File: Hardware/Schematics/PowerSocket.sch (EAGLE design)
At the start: 74 parts, among them T1 BT138-V, T2 BT138-V, T3 BT138-V, T4 BT138-V, T5 BT138-V, T6 BT138-V

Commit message: New board layout
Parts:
- removed ACIN-NULL, ACIN-PHASE, ACOUT-NULL, ACOUT-NULL1, ACOUT-NULL2, ACOUT-PHASE, ACOUT-PHASE1, ACOUT-PHASE2: -, wirepad:3,81/1,4
- removed BUTTON_LED+: BUTTON_VCC, wirepad:2,15/1,0
- removed BUTTON_LED+1, BUTTON_LED+2, BUTTON_LED-, BUTTON_LED-1, BUTTON_LED-2, BUTTON_SWITCH1, BUTTON_SWITCH3, BUTTON_SWITCH5: -, wirepad:2,15/1,0
- removed U$1, U$3, U$4: ACS710, PowerSocket:ACS710
- added AMP1, AMP2, AMP3: ACS710, PowerSocket:ACS710
- added BUTTON1_VCC: (no value), wirepad:2,15/1,0
- added BUTTON2_VCC, BUTTON3_VCC, LED1, LED2, LED3, SWITCH1, SWITCH2, SWITCH3: -, wirepad:2,15/1,0
- added NULL, NULL1-OUT, NULL2-OUT, NULL3-OUT, PHASE, PHASE1-OUT, PHASE2-OUT, PHASE3-OUT: -, wirepad:3,81/1,4
- added R24: 0, eagle-ltspice:RR2010
- R14, R18: device rcl:C-EUC0805 -> rcl:R-EU_R0805
- T1, T2, T3, T4, T5, T6: value BT138-V -> BT138-H; device triac:BT138-V -> triac:BT138-H
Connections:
- net N$25 renamed GATE2
- net N$3 renamed VOLTMETER
- removed net N$15 (its old number): BUTTON_LED-.P, R7.1
- removed net N$2 (its old number): R1.1, RESET.P1, U$2.EN
- removed net N$36 (its old number): ACOUT-PHASE1.P, U$3.IP-, U$3.IP-1, U$3.IP-2, U$3.IP-3
- removed net N$40: U$3.NFAULT
- removed net N$42 (its old number): OK5.C, R16.2
- removed net N$43: OK5.A2, R17.1
- removed net N$45: ACIN-NULL.P, R5.1, T1.A1, T3.A1, T5.A1
- removed net N$46: OK6.C, R18.1
- removed net N$47: OK6.A2, R19.1
- removed net N$49: R19.2, T6.A2, U$4.IP+, U$4.IP+1, U$4.IP+2, U$4.IP+3
- removed net N$50: U$4.NFAULT
- removed net N$51: ACIN-PHASE.P, D1.C, T2.A1, T4.A1, T6.A1
- removed net N$52: R22.2, U$2.IO5
- removed net N$53: R15.2, T4.A2, U$3.IP+, U$3.IP+1, U$3.IP+2, U$3.IP+3
- removed net N$54: R16.1, R18.2, U$2.IO27
- removed net N$55: C9.2, U$1.FILTER
- removed net N$60: C10.2, U$1.VZCR
- removed net N$62: C1.2, U$3.FILTER
- removed net N$63: C4.2, U$3.VZCR
- removed net N$64: C5.2, U$4.FILTER
- removed net N$65: C6.2, U$4.VZCR
- new net AMP1: AMP1.VIOUT, U$2.IO34
- new net AMP2: AMP2.VIOUT, U$2.IO35
- new net AMP3: AMP3.VIOUT, U$2.IO32
- new net BUTTON1: R8.1, SWITCH1.P, U$2.IO22
- new net BUTTON2: R21.1, SWITCH2.P, U$2.IO23
- new net BUTTON3: R23.1, SWITCH3.P, U$2.IO5
- new net GATE1: R3.2, R9.2, U$2.IO25
- new net GATE3: R16.1, R18.1, U$2.IO27
- new net LED1: R7.2, U$2.IO19
- new net LED2: R20.2, U$2.IO18
- new net LED3: R22.2, U$2.IO17
- new net N$24: FLASH.P, FLASH.P1, R2.2, U$2.IO0
- new net N$30: AMP2.VZCR, C4.1
- new net N$66: R1.1, RESET.P, RESET.P1, U$2.EN
- new net NULL: NULL.P, R5.1, T2.A1, T4.A1, T6.A1
- new net PHASE: PHASE.P, R24.2, T1.A1, T3.A1, T5.A1
- new net PHASE1: AMP1.IP+, AMP1.IP+1, AMP1.IP+2, AMP1.IP+3, R10.2, T1.A2
- new net PHASE2: AMP2.IP+, AMP2.IP+1, AMP2.IP+2, AMP2.IP+3, R15.2, T3.A2
- new net PHASE3: AMP3.IP+, AMP3.IP+1, AMP3.IP+2, AMP3.IP+3, R19.2, T5.A2
- net GND: now also AMP1.FAULT_EN, AMP1.GND, AMP2.FAULT_EN, AMP2.GND, AMP3.FAULT_EN, AMP3.GND, C1.2, C10.2, C11.2, C12.2, C13.2, C4.2, C5.2, C6.2, C9.2, FLASH.S, R21.2, R23.2, R8.2, RESET.S1; no longer C1.1, C10.1, C11.1, C12.1, C13.1, C4.1, C5.1, C6.1, C9.1, R21.1, R23.1, R8.1, U$1.FAULT_EN, U$1.GND, U$3.FAULT_EN, U$3.GND, U$4.FAULT_EN, U$4.GND
- net N$1: now also OK1.C, R9.1; no longer ACOUT-NULL.P, R4.2, T1.A2
- net N$10: now also AMP3.IP-, AMP3.IP-1, AMP3.IP-2, AMP3.IP-3, PHASE3-OUT.P; no longer OK2.C, R9.1
- net N$11: now also LED3.P, R22.1; no longer U$2.IO35, U$3.VIOUT
- net N$12: now also AMP1.VZCR, C10.1; no longer U$1.VIOUT, U$2.IO34
- net N$13: now also AMP1.FILTER, C9.1; no longer ACOUT-PHASE.P, U$1.IP-, U$1.IP-1, U$1.IP-2, U$1.IP-3
- net N$14: now also NULL2-OUT.P, T4.A2; no longer ACOUT-NULL1.P, T3.A2
- net N$16: now also OK4.A2, R13.1; no longer BUTTON_LED-1.P, R20.1
- net N$17: now also NULL1-OUT.P, R4.2, T2.A2; no longer BUTTON_SWITCH1.P, R8.2, U$2.IO19
- net N$18: now also OK5.C, R18.2; no longer OK1.A2, R4.1
- net N$20: now also OK1.A2, R10.1; no longer BUTTON_SWITCH3.P, R21.2, U$2.IO18
- net N$21: now also R4.1; no longer R10.1
- net N$23: now also OK3.A2, R15.1; no longer R10.2, T2.A2, U$1.IP+, U$1.IP+1, U$1.IP+2, U$1.IP+3
- net N$26: now also AMP2.IP-, AMP2.IP-1, AMP2.IP-2, AMP2.IP-3, PHASE2-OUT.P; no longer BUTTON_LED-2.P, R22.1
- net N$27: now also AMP1.IP-, AMP1.IP-1, AMP1.IP-2, AMP1.IP-3, PHASE1-OUT.P; no longer U$1.NFAULT
- net N$28: now also R14.1; no longer R12.2
- net N$29: now also OK4.C, R12.2; no longer OK3.A2, R13.1
- net N$31: now also OK6.C, R16.2; no longer R20.2, U$2.IO23
- net N$32: now also AMP2.FILTER, C1.1; no longer OK4.C, R14.1
- net N$33: now also OK6.A2, R17.1; no longer OK4.A2, R15.1
- net N$35: now also OK5.A2, R19.1; no longer ACOUT-PHASE2.P, U$4.IP-, U$4.IP-1, U$4.IP-2, U$4.IP-3
- net N$38: now also AMP3.VZCR, C6.1; no longer ACOUT-NULL2.P, R17.2, T5.A2
- net N$39: now also AMP3.FILTER, C5.1; no longer BUTTON_SWITCH5.P, R23.2, U$2.IO17
- net N$41: now also D1.C, R24.1; no longer U$2.IO32, U$4.VIOUT
- net N$6: now also OK2.C, R3.1; no longer OK1.C, R3.2
- net N$7: now also LED2.P, R20.1; no longer FLASH.P, R2.2, U$2.IO0
- net N$8: now also NULL3-OUT.P, R17.2, T6.A2; no longer R3.1, R9.2, U$2.IO25
- net N$9: now also LED1.P, R7.1; no longer R7.2, U$2.IO22
- net VCC: now also AMP1.VCC, AMP1.VOC, AMP2.VCC, AMP2.VOC, AMP3.VCC, AMP3.VOC, BUTTON1_VCC.P, BUTTON2_VCC.P, BUTTON3_VCC.P, C11.1, C12.1, C13.1; no longer BUTTON_LED+.P, BUTTON_LED+1.P, BUTTON_LED+2.P, C11.2, C12.2, C13.2, U$1.VCC, U$1.VOC, U$3.VCC, U$3.VOC, U$4.VCC, U$4.VOC
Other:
- moved on the sheet: C1, C10, C11, C12, C13, C2, C3, C4, C5, C6, C9, D1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

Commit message: Added .brd script.
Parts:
- removed BUTTON1_VCC: (no value), wirepad:2,15/1,0
- removed BUTTON2_VCC, BUTTON3_VCC, LED1, LED2, LED3, SWITCH1, SWITCH2, SWITCH3: -, wirepad:2,15/1,0
- added BUTTON1, BUTTON2, BUTTON3: (no value), pinhead:PINHD-1X3
- renumbered U$2 to ESP3212
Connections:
- removed net N$24: ESP3212.IO0, FLASH.P, FLASH.P1, R2.2
- new net FLASH: ESP3212.IO25, FLASH.P, FLASH.P1, R2.2
- net BUTTON1: now also BUTTON1.3; no longer SWITCH1.P
- net BUTTON2: now also BUTTON2.3; no longer SWITCH2.P
- net BUTTON3: now also BUTTON3.3; no longer SWITCH3.P
- net GATE1: now also ESP3212.IO0; no longer ESP3212.IO25
- net GATE2: now also ESP3212.IO4; no longer ESP3212.IO26
- net GATE3: now also ESP3212.IO16; no longer ESP3212.IO27
- net N$11: now also BUTTON3.2; no longer LED3.P
- net N$7: now also BUTTON2.2; no longer LED2.P
- net N$9: now also BUTTON1.2; no longer LED1.P
- net VCC: now also BUTTON1.1, BUTTON2.1, BUTTON3.1; no longer BUTTON1_VCC.P, BUTTON2_VCC.P, BUTTON3_VCC.P
- net VOLTMETER: now also ESP3212.IO26; no longer ESP3212.IO4
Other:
- moved on the sheet: FLASH, JTAG, R2, R21, R23, R8

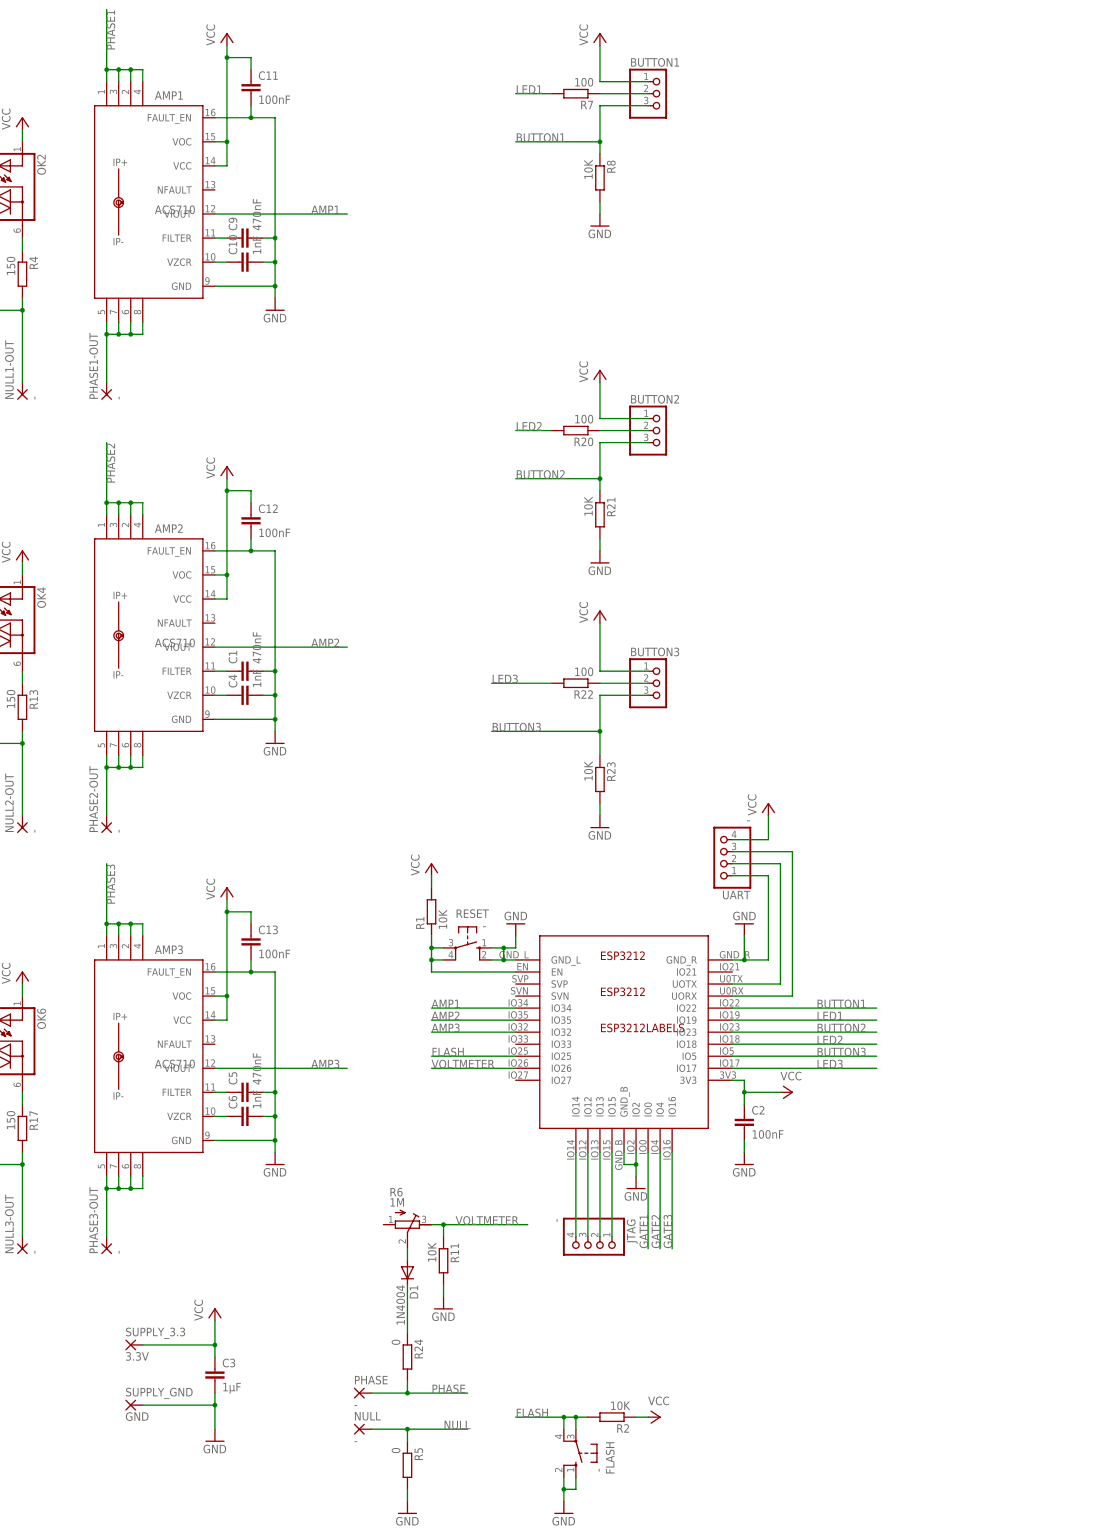
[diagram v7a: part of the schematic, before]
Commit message: Changed amp-meters and added 5V step-up. I probably don't have the correct package.
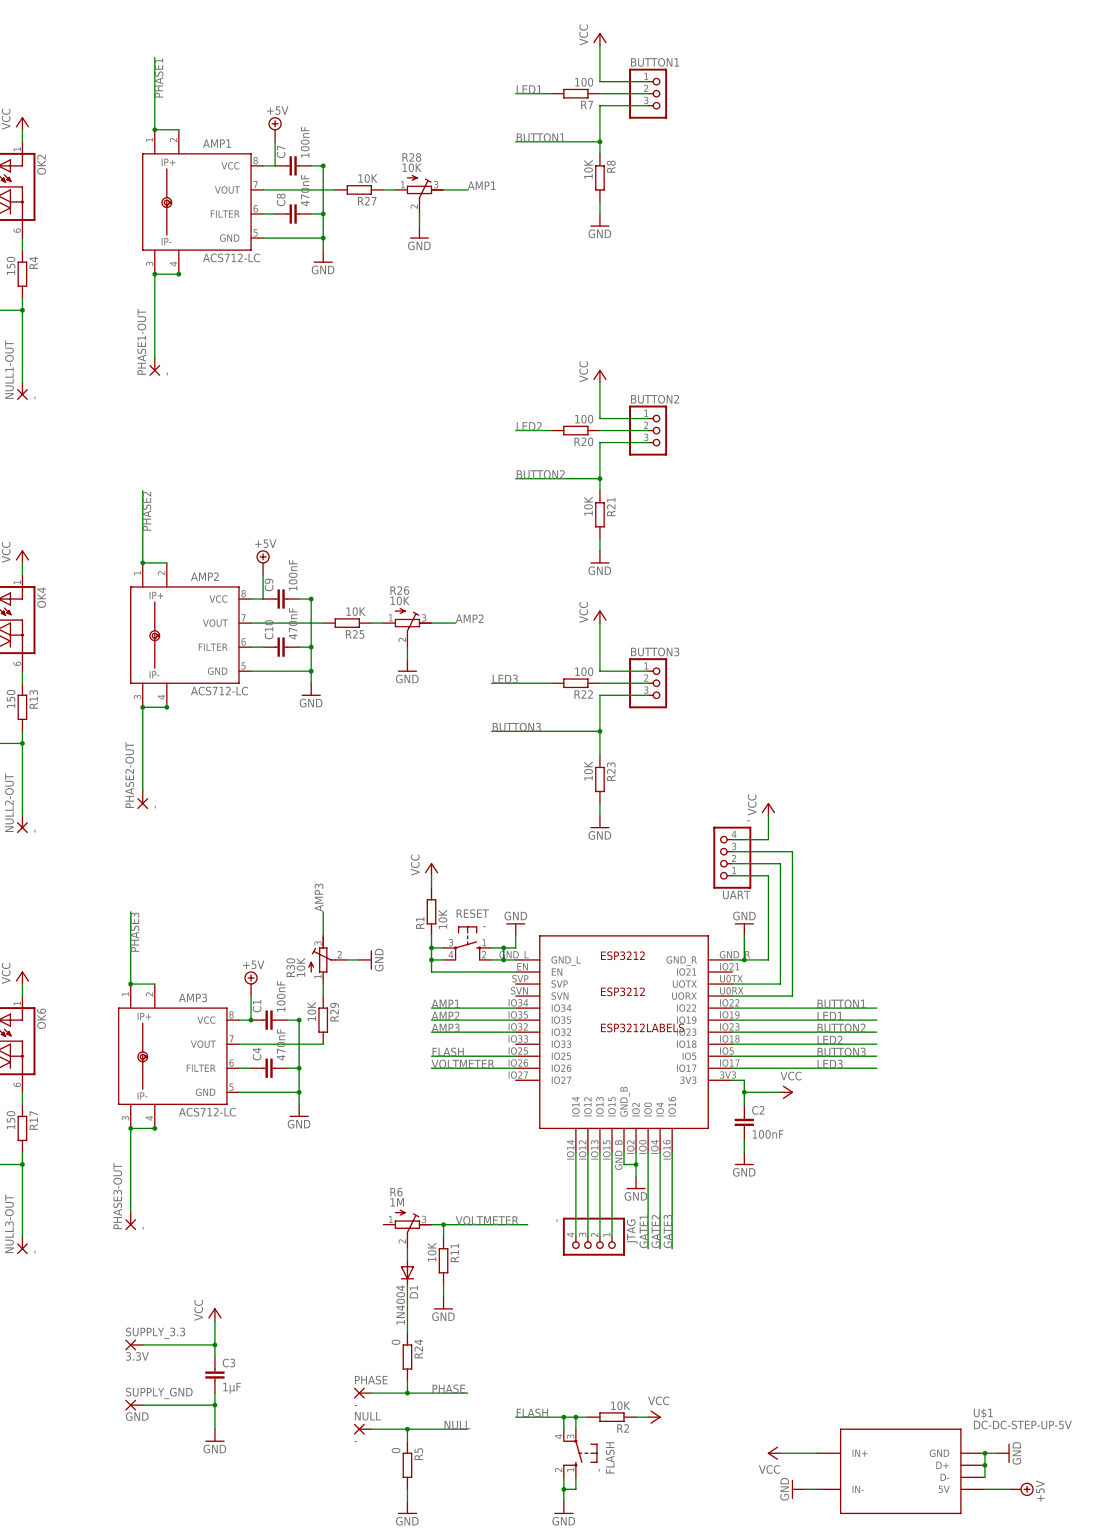
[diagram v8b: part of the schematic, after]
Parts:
- removed C11, C12, C13: 100nF, rcl:C-EUC0805
- removed C5: 470nF, rcl:C-EUC0805
- removed C6: 1nF, rcl:C-EUC0805
- added C7: 100nF, rcl:C-EUC0805
- added C8: 470nF, rcl:C-EUC0805
- added R25, R27, R29: 10K, rcl:R-EU_R0805
- added R26, R28, R30: 10K, rcl:R-TRIMM5X
- added U$1: DC-DC-STEP-UP-5V, diy-modules:DC-DC-STEP-UP-5V
- AMP1, AMP2, AMP3: value ACS710 -> ACS712-LC; device PowerSocket:ACS710 -> allegro-2:ACS712-LC
- C1, C9: value 470nF -> 100nF
- C10, C4: value 1nF -> 470nF
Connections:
- removed net N$30: AMP2.VZCR, C4.1
- removed net N$32: AMP2.FILTER, C1.1
- new net +5V: AMP1.VCC, AMP2.VCC, AMP3.VCC, C1.1, C7.1, C9.1, U$1.5V
- new net N$24: AMP1.FILTER, C8.1
- new net N$37: AMP2.VOUT, R25.2
- new net N$40: R29.1, R30.A
- new net N$43: AMP3.VOUT, R29.2
- new net N$44: AMP1.VOUT, R27.2
- net AMP1: now also R28.E; no longer AMP1.VIOUT
- net AMP2: now also R26.E; no longer AMP2.VIOUT
- net AMP3: now also R30.E; no longer AMP3.VIOUT
- net GND: now also C7.2, C8.2, R26.S, R28.S, R30.S, U$1.D+, U$1.D-, U$1.GND, U$1.IN-; no longer AMP1.FAULT_EN, AMP2.FAULT_EN, AMP3.FAULT_EN, C11.2, C12.2, C13.2, C5.2, C6.2
- net N$10: no longer AMP3.IP-2, AMP3.IP-3
- net N$12: now also AMP2.IP-, AMP2.IP-1, PHASE2-OUT.P; no longer AMP1.VZCR, C10.1
- net N$13: now also AMP2.FILTER, C10.1; no longer AMP1.FILTER, C9.1
- net N$26: now also AMP3.FILTER, C4.1; no longer AMP2.IP-, AMP2.IP-1, AMP2.IP-2, AMP2.IP-3, PHASE2-OUT.P
- net N$27: no longer AMP1.IP-2, AMP1.IP-3
- net N$38: now also R25.1, R26.A; no longer AMP3.VZCR, C6.1
- net N$39: now also R27.1, R28.A; no longer AMP3.FILTER, C5.1
- net PHASE1: no longer AMP1.IP+2, AMP1.IP+3
- net PHASE2: no longer AMP2.IP+2, AMP2.IP+3
- net PHASE3: no longer AMP3.IP+2, AMP3.IP+3
- net VCC: now also U$1.IN+; no longer AMP1.VCC, AMP1.VOC, AMP2.VCC, AMP2.VOC, AMP3.VCC, AMP3.VOC, C11.1, C12.1, C13.1
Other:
- moved on the sheet: C1, C10, C4, C9, PHASE1-OUT, PHASE2-OUT, PHASE3-OUT
